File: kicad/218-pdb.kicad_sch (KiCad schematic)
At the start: 72 parts, among them J1 Conn_01x03, J10 Conn_01x03, J11 Conn_01x03, J12 Conn_01x03, J13 Conn_01x03, J14 Conn_01x03, J15 Conn_01x03, J16 Conn_01x03, J17 Conn_01x03, J18 Conn_01x03, J19 Conn_01x03, J2 Conn_01x03, J20 Conn_01x03, J21 Conn_01x03, J22 Conn_01x03, J23 Conn_01x03, J24 Conn_01x03, J25 Conn_01x04_Pin, J26 Conn_01x04_Pin, J27 external 5V, J28 battery, J29 battery, J3 Conn_01x03, J30 battery, J31 battery, J32 battery, J33 battery, J4 Conn_01x03, J5 Conn_01x03, J6 Conn_01x03, J7 Conn_01x03, J8 Conn_01x03, J9 Conn_01x03, SW1 5V switch, U1 3.3V 0.5A LDO, U2 DC-DC buck, U3 3.3V 0.5A LDO, U4 DC-DC buck, U5 5V 1.0A LDO

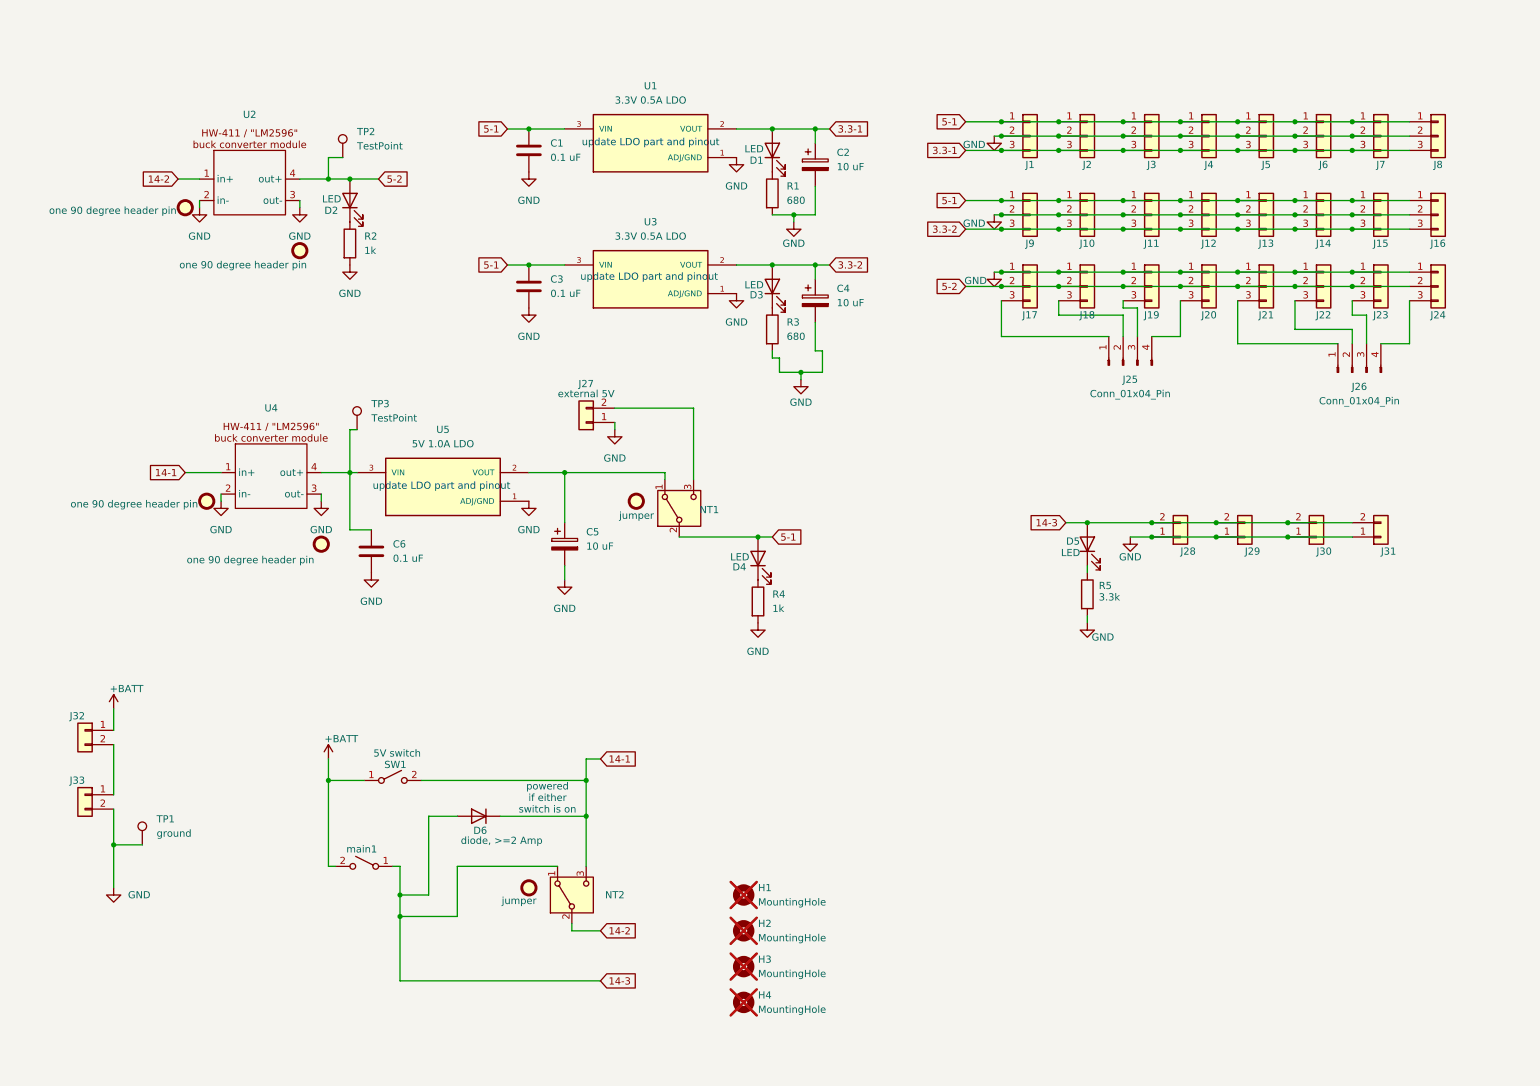
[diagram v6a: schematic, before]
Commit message: change schematic and start layout
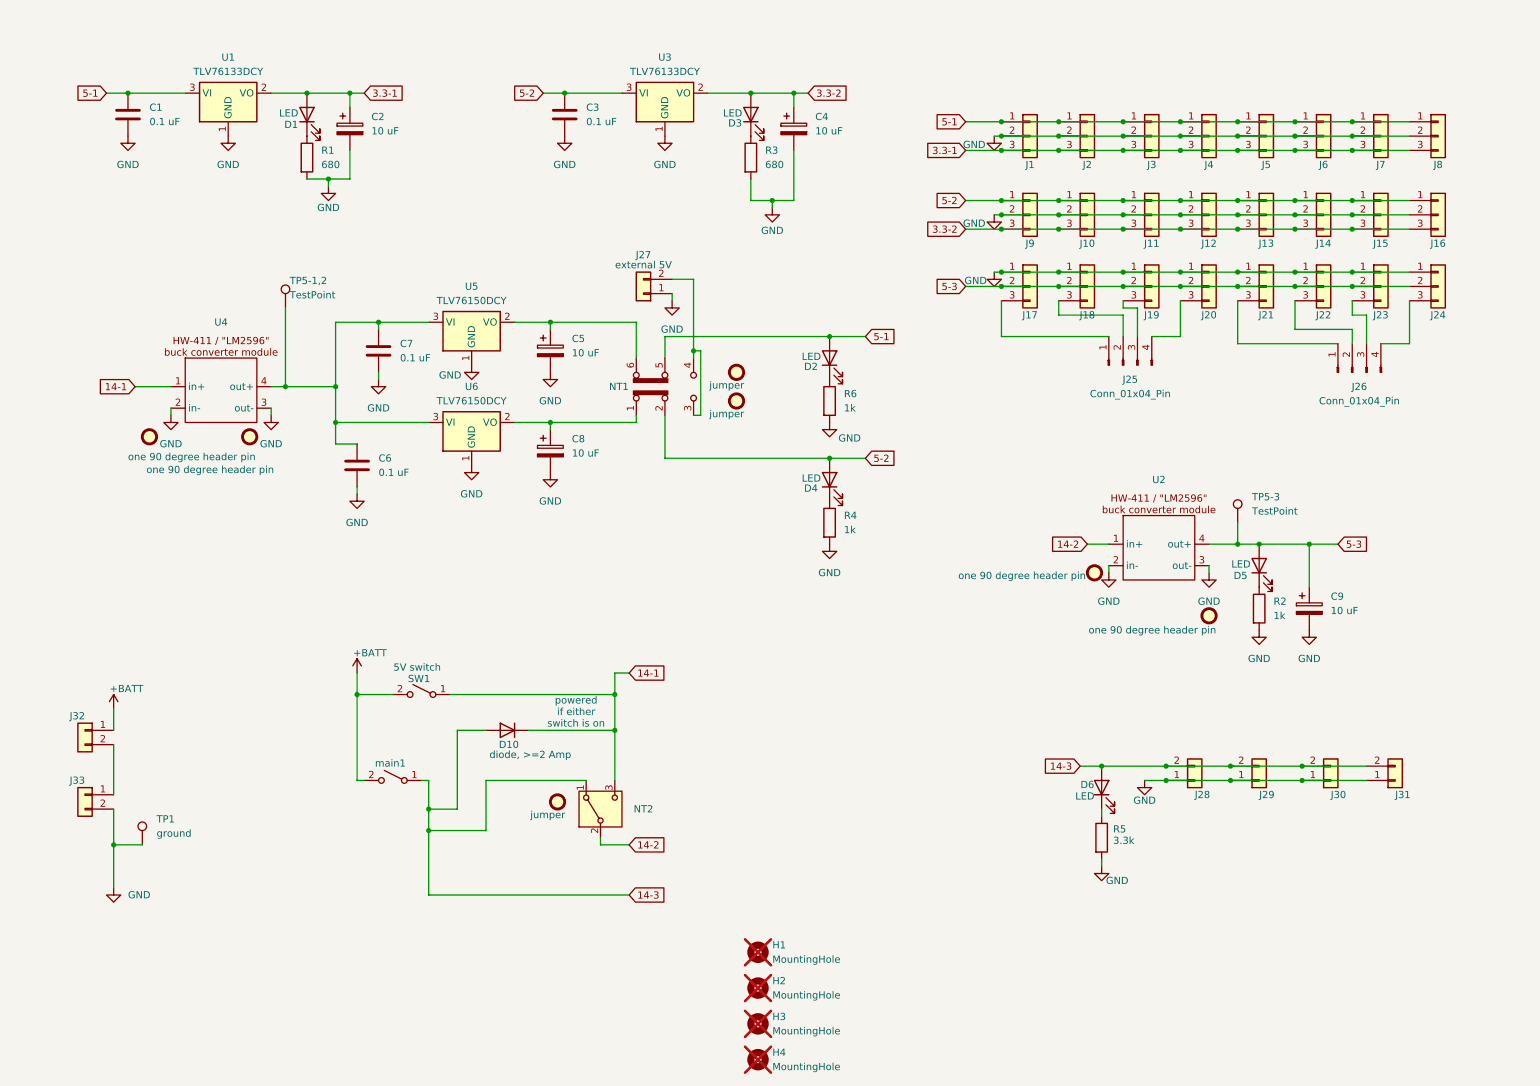
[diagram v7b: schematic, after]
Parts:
- removed FID9: jumper, 218-pdb:jumper, symbol Mechanical:Fiducial
- removed NT1: ~, 218-pdb:PinHeader_1x03_P2.54mm_Vertical, symbol Switch:SW_SPDT
- removed U1, U3: 3.3V 0.5A LDO, Package_TO_SOT_THT:TO-220-3_Vertical, symbol 218-pdb:LD1117V33
- removed U5: 5V 1.0A LDO, Package_TO_SOT_THT:TO-220-3_Vertical, symbol 218-pdb:LD1117V33
- added C7: 0.1 uF, Capacitor_THT:C_Disc_D3.0mm_W2.0mm_P2.50mm, symbol Device:C
- added C8, C9: 10 uF, Capacitor_THT:C_Disc_D3.8mm_W2.6mm_P2.50mm, symbol Device:C_Polarized
- added D2: LED, 218-pdb:LED_D3.0mm, symbol Device:LED
- added FID5, FID6: jumper, 218-pdb:jumper, symbol Mechanical:Fiducial
- added NT1: SW_Slide_DPDT, 218-pdb:PinHeader_2x03_P2.54mm_Vertical, symbol Switch:SW_Slide_DPDT
- added R6: 1k, Resistor_THT:R_Axial_DIN0309_L9.0mm_D3.2mm_P2.54mm_Vertical, symbol Device:R
- added U1, U3: TLV76133DCY, Package_TO_SOT_SMD:SOT-223-3_TabPin2, symbol Regulator_Linear:TLV76133DCY
- added U5, U6: TLV76150DCY, Package_TO_SOT_SMD:SOT-223-3_TabPin2, symbol Regulator_Linear:TLV76150DCY
- SW1: footprint (none) -> 218-pdb:1101A4CQEA; Manufacturer_Name (none) -> CIT Relay and Switch; Part_Number ANT11SF1CQE -> 1101A4CQEA; digikey_part_number (none) -> 2449-1101A4CQEA-ND
- TP5-1,2: renamed from TP3; footprint (none) -> TestPoint:TestPoint_THTPad_D2.0mm_Drill1.0mm
- TP5-3: renamed from TP2; footprint (none) -> TestPoint:TestPoint_THTPad_D2.0mm_Drill1.0mm
- renumbered D6 to D10, D2 to D5, D5 to D6, FID4 to FID1, FID3 to FID2, FID1 to FID3, FID2 to FID4
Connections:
- net +BATT: now also SW1.2 (B); no longer SW1.1 (A)
- net 14-1: now also SW1.1 (A); no longer SW1.2 (B)
- net 3.3-1: now also U1.2 (VO)
- net 3.3-2: now also U3.2 (VO)
- net 5-1: now also D2.2 (A), NT1.5 (B), U1.3 (VI); no longer C3.1, D4.2 (A), J10.1 (Pin_1), J11.1 (Pin_1), J12.1 (Pin_1), J13.1 (Pin_1), J14.1 (Pin_1), J15.1 (Pin_1), J16.1 (Pin_1), J9.1 (Pin_1)
- net 5-2: now also C3.1, D4.2 (A), J10.1 (Pin_1), J11.1 (Pin_1), J12.1 (Pin_1), J13.1 (Pin_1), J14.1 (Pin_1), J15.1 (Pin_1), J16.1 (Pin_1), J9.1 (Pin_1), NT1.2 (B), U3.3 (VI); no longer D5.2 (A), J17.2 (Pin_2), J18.2 (Pin_2), J19.2 (Pin_2), J20.2 (Pin_2), J21.2 (Pin_2), J22.2 (Pin_2), J23.2 (Pin_2), J24.2 (Pin_2), TP5-3.1, U2.4 (out+)
- net GND: now also C7.2, C8.2, C9.2, R6.2, U1.1 (GND), U3.1 (GND), U5.1 (GND), U6.1 (GND)
- net at C6.1, TP5-1,2.1, U4.4 (out+): now also C7.1, U5.3 (VI), U6.3 (VI)
- net at C5.1: now also NT1.6 (C), U5.2 (VO)
- net at J27.2 (Pin_2): now also NT1.3 (C), NT1.4 (A)
- new net: D2.1 (K), R6.1
- new net: C8.1, NT1.1 (A), U6.2 (VO)
- new net 5-3: C9.1, D5.2 (A), J17.2 (Pin_2), J18.2 (Pin_2), J19.2 (Pin_2), J20.2 (Pin_2), J21.2 (Pin_2), J22.2 (Pin_2), J23.2 (Pin_2), J24.2 (Pin_2), TP5-3.1, U2.4 (out+)
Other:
- note removed: "update LDO part and pinout"
- moved on the sheet: C1, C2, C3, C4, C5, C6, D1, D10, D3, D4, D5, D6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

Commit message: add traces
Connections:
- net GND: now also R2.1; no longer R2.2
- net at D5.1 (K): now also R2.2; no longer R2.1
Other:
- moved on the sheet: C6, R2
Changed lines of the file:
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@@
 		(rev "2.1 E")
 		(comment 1 "SPDL")
-		(comment 2 "by Joshua Phelps joshuaphelps127@gmail.com joshua18@stanford.edu")
+		(comment 2 "by Joshua Phelps 2026 joshua18@stanford.edu joshua262144@gmail.com")
 		(comment 3 "Stanford ME218")
 	)
@@
 	(wire
 		(pts
-			(xy 71.12 97.79) (xy 71.12 96.52)
+			(xy 67.31 97.79) (xy 67.31 96.52)
 		)
 		(stroke
@@
 	(wire
 		(pts
-			(xy 71.12 88.9) (xy 67.31 88.9)
-		)
-		(stroke
-			(width 0)
-			(type default)
-		)
-	)
-	(wire
-		(pts
 			(xy 237.49 50.8) (xy 247.65 50.8)
 		)
@@
 	(symbol
 		(lib_id "Device:R")
-		(at 231.14 118.11 0)
+		(at 231.14 118.11 180)
 		(unit 1)
 		(exclude_from_sim no)
@@
 					(size 1.27 1.27)
 				)
-				(justify left)
+				(justify right)
 			)
 		)
@@
 					(size 1.27 1.27)
 				)
-				(justify left)
+				(justify right)
 			)
 		)
 		(property "Footprint" "Resistor_THT:R_Axial_DIN0309_L9.0mm_D3.2mm_P2.54mm_Vertical"
-			(at 229.362 118.11 90)
+			(at 232.918 118.11 90)
 			(effects
 				(font
@@
 	(symbol
 		(lib_id "power:GND")
-		(at 71.12 97.79 0)
+		(at 67.31 97.79 0)
 		(unit 1)
 		(exclude_from_sim no)
@@
 		(fields_autoplaced yes)
 		(property "Reference" "#PWR023"
-			(at 71.12 104.14 0)
+			(at 67.31 104.14 0)
 			(effects
 				(font
@@
 		)
 		(property "Value" "GND"
-			(at 71.12 102.87 0)
+			(at 67.31 102.87 0)
 			(effects
 				(font
@@
 		)
 		(property "Footprint" ""
-			(at 71.12 97.79 0)
+			(at 67.31 97.79 0)
 			(effects
 				(font
@@
 		)
 		(property "Datasheet" ""
-			(at 71.12 97.79 0)
+			(at 67.31 97.79 0)
 			(effects
 				(font
@@
 		)
 		(property "Description" "Power symbol creates a global label with name \"GND\" , ground"
-			(at 71.12 97.79 0)
+			(at 67.31 97.79 0)
 			(effects
 				(font
@@
 	(symbol
 		(lib_id "Device:C")
-		(at 71.12 92.71 0)
+		(at 67.31 92.71 0)
 		(unit 1)
 		(exclude_from_sim no)
@@
 		(fields_autoplaced yes)
 		(property "Reference" "C6"
-			(at 74.93 91.4399 0)
+			(at 71.12 91.4399 0)
 			(effects
 				(font
@@
 		)
 		(property "Value" "0.1 uF"
-			(at 74.93 93.9799 0)
+			(at 71.12 93.9799 0)
 			(effects
 				(font
@@
 		)
 		(property "Footprint" "Capacitor_THT:C_Disc_D3.0mm_W2.0mm_P2.50mm"
-			(at 72.0852 96.52 0)
+			(at 68.2752 96.52 0)
 			(effects
 				(font
@@
 		)
 		(property "Datasheet" "~"
-			(at 71.12 92.71 0)
+			(at 67.31 92.71 0)
 			(effects
 				(font
@@
 		)
 		(property "Description" "Unpolarized capacitor"
-			(at 71.12 92.71 0)
+			(at 67.31 92.71 0)
 			(effects
 				(font
@@
 		)
 		(property "Manufacturer_Name" ""
-			(at 71.12 92.71 0)
+			(at 67.31 92.71 0)
 			(effects
 				(font
@@
 		)
 		(property "digikey_part_number" ""
-			(at 71.12 92.71 0)
+			(at 67.31 92.71 0)
 			(effects
 				(font
@@
 		)
 		(property "mount_type" "tht"
-			(at 71.12 92.71 0)
+			(at 67.31 92.71 0)
 			(effects
 				(font
@@
 		)
 		(property "Part_Number" "0.1 uF ceramic capacitor"
-			(at 71.12 92.71 0)
+			(at 67.31 92.71 0)
 			(effects
 				(font
